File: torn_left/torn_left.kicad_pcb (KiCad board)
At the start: 2 copper layers, 140.7 x 115.6 mm, 76 parts, among them J1 SJ-43514, SW1 SW_Push, SW10 SW_Push, SW11 SW_Push, SW12 SW_Push, SW13 SW_Push, SW14 SW_Push, SW15 SW_Push, SW16 SW_Push, SW17 SW_Push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

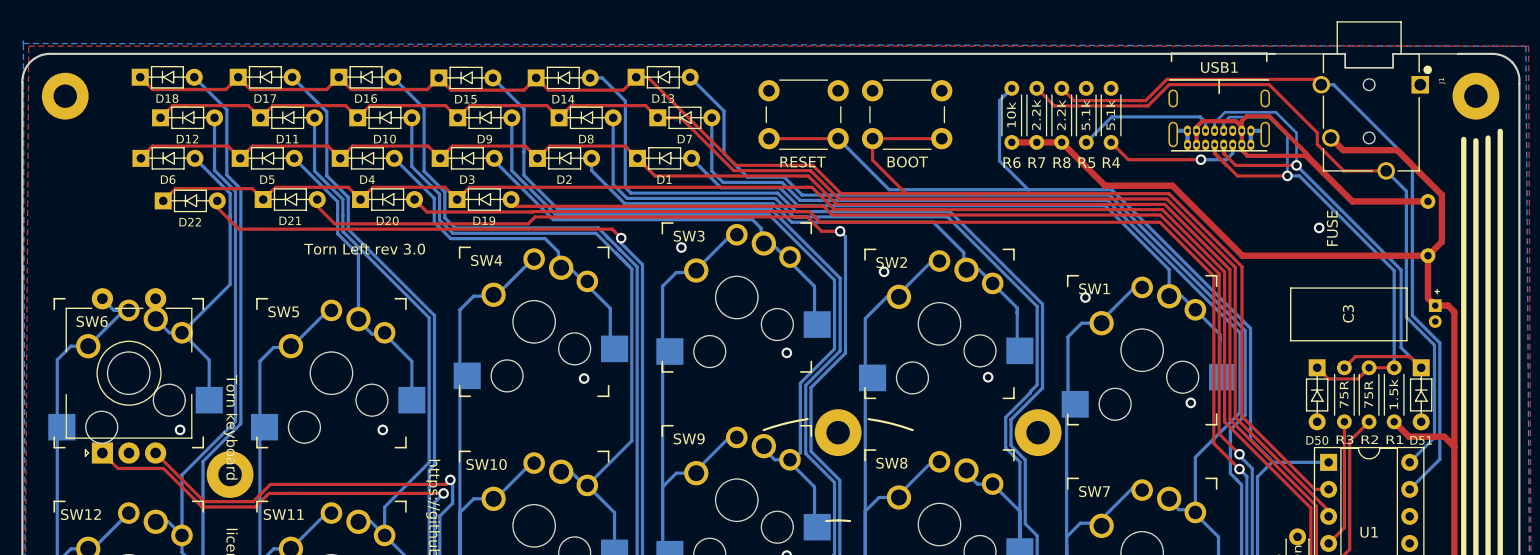
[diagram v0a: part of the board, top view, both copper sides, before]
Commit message: switched out SJ-43514 TRRS jack connector for PJ-320A
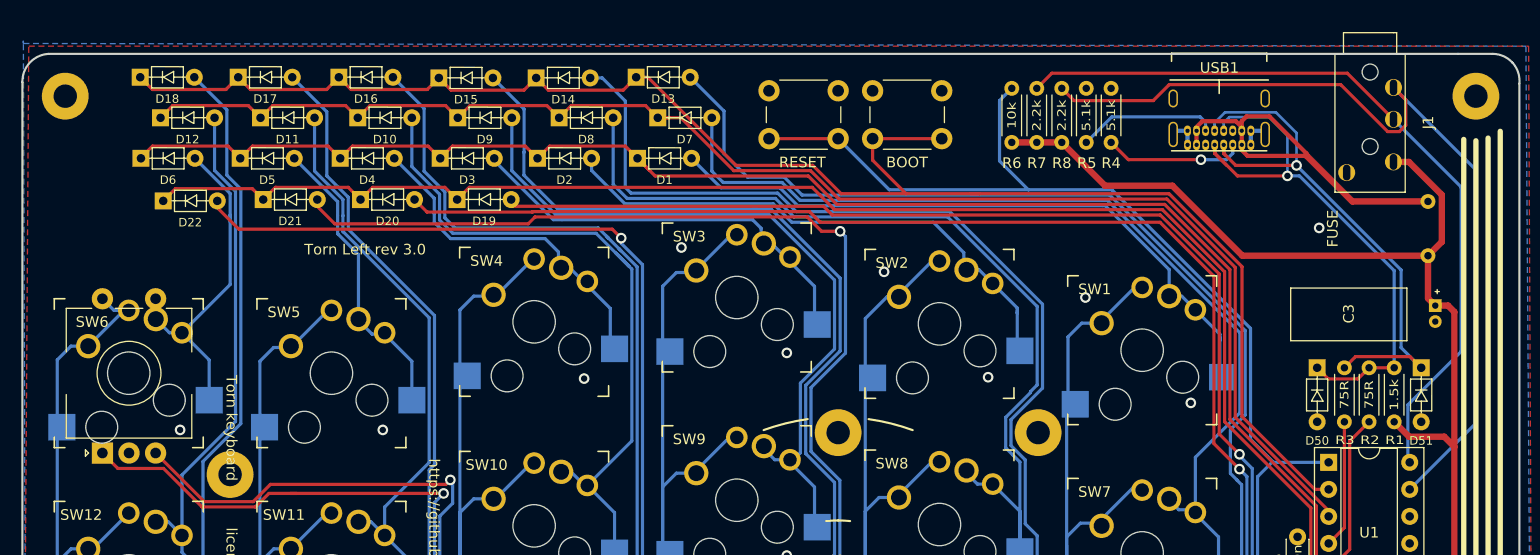
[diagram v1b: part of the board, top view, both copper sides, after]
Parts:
- J1: footprint footprints:CUI_SJ-43514 -> footprints:PJ-320A
- moved J1 7.83 mm to (179.1, 48.3)
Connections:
- U1 pad 21: (no net) -> Net-(U1-Pad21)
- U1 pad 23: (no net) -> Net-(U1-Pad23)
- U1 pad 24: (no net) -> Net-(U1-Pad24)
- U1 pad 25: (no net) -> Net-(U1-Pad25)
- U1 pad 26: (no net) -> Net-(U1-Pad26)
- USB1 pad A8: (no net) -> Net-(USB1-PadA8)
- USB1 pad B8: (no net) -> Net-(USB1-PadB8)
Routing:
- net /i2c_SDA: track 70.4 -> 83.0 mm
- net +5V: track 151.9 -> 145.1 mm
- net /i2c_SCL: track 68.6 -> 72.9 mm
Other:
- outline, holes or cut-outs redrawn
